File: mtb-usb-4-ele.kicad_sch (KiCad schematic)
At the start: 76 parts, among them J1 USB_C_Receptacle_USB2.0, J2 PROG/DEBUG, J3 Conn_01x06, J4 RJ12, J5 RJ12, J6 Screw_Terminal_01x02, J7 Screw_Terminal_01x02, J8 Conn_01x02, U1 STM32F103C8Tx, U2 AMS1117-3.3, U3 ADM2483xRW, U4 ADUM1250, U6 LM78M05_TO252, U7 INA219AxDCN, Y1 8 MHz

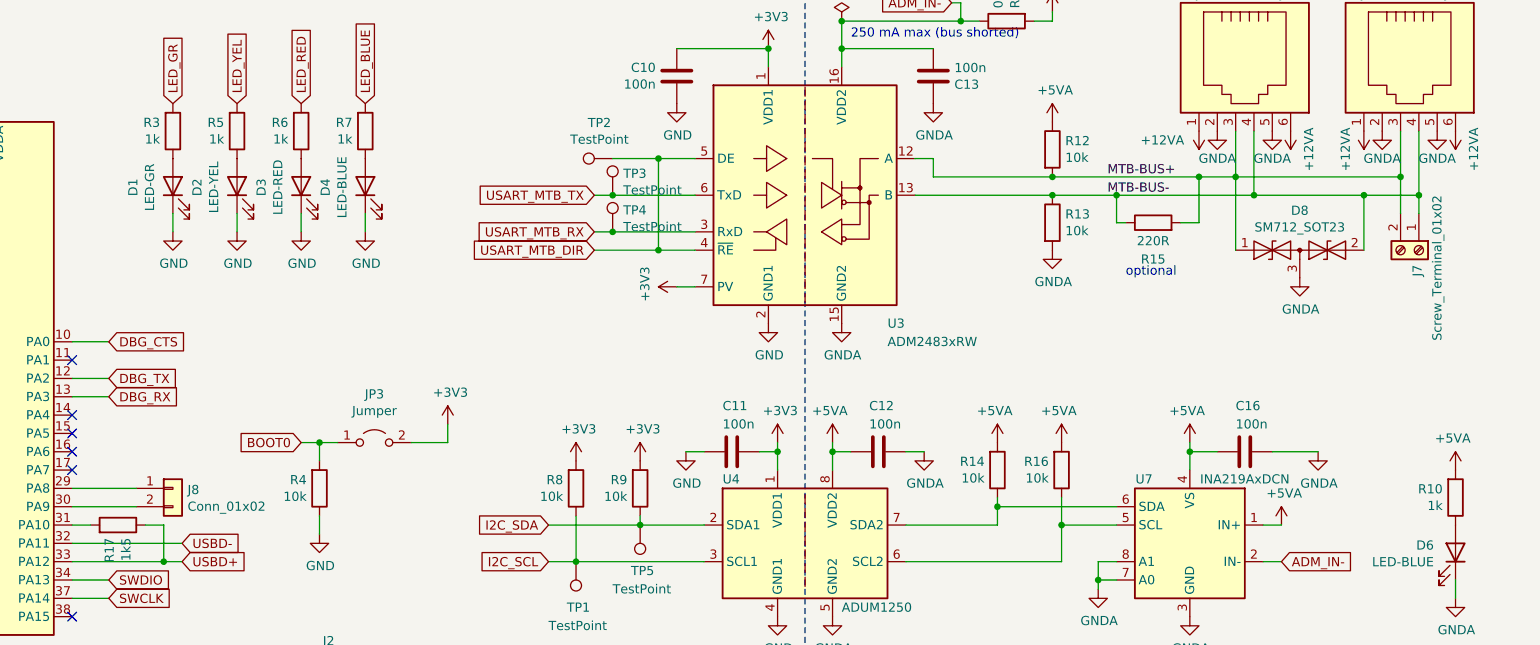
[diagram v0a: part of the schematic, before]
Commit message: Adjust LED resistors.
* 5V blue: 4k7.
* 3V3 blue: 2k2.
* 3V3 green: 10k.
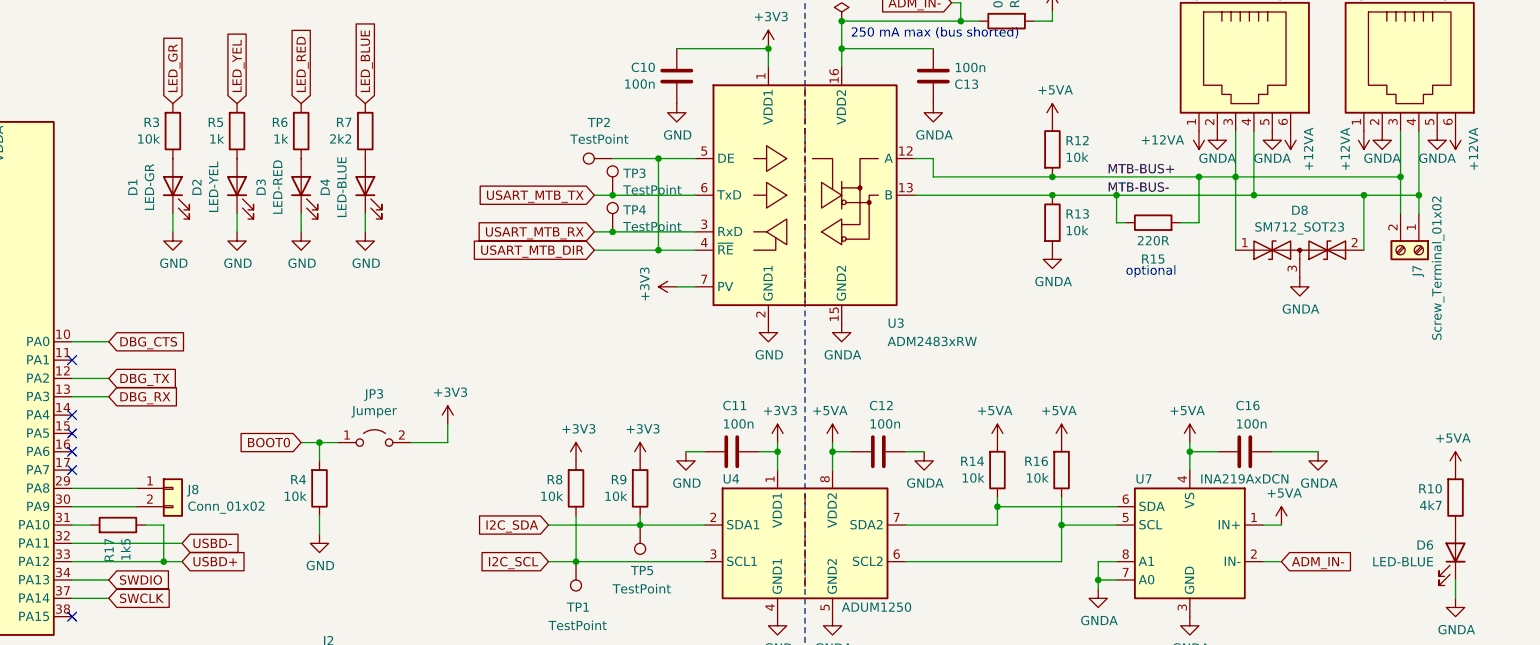
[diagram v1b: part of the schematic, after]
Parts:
- R10: value 1k -> 4k7; LCSC C17513 -> C17673
- R3: value 1k -> 10k; LCSC C17513 -> C17414
- R7: value 1k -> 2k2; LCSC C17513 -> C17520
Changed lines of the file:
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@@
 			)
 		)
-		(property "Value" "1k"
+		(property "Value" "10k"
 			(at 98.552 36.703 0)
 			(effects
@@
 			)
 		)
-		(property "LCSC" "C17513"
+		(property "LCSC" "C17414"
 			(at 100.33 35.56 0)
 			(effects
@@
 			)
 		)
-		(property "Value" "1k"
+		(property "Value" "2k2"
 			(at 125.222 36.703 0)
 			(effects
@@
 			)
 		)
-		(property "LCSC" "C17513"
+		(property "LCSC" "C17520"
 			(at 127 35.56 0)
 			(effects
@@
 			)
 		)
-		(property "Value" "1k"
+		(property "Value" "4k7"
 			(at 276.352 87.503 0)
 			(effects
@@
 			)
 		)
-		(property "LCSC" "C17513"
+		(property "LCSC" "C17673"
 			(at 278.13 86.36 0)
 			(effects

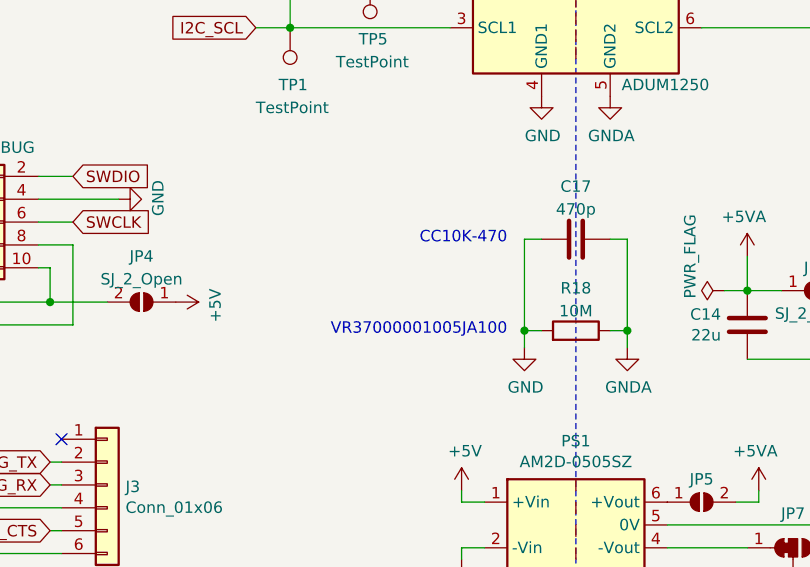
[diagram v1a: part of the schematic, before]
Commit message: TME part id as a part's property.
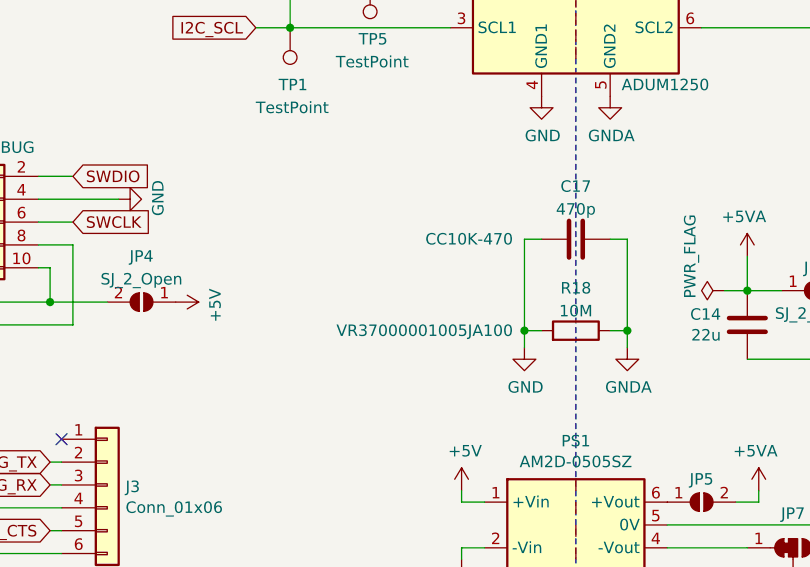
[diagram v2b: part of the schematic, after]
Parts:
- C17: TME (none) -> CC10K-470
- R18: TME (none) -> VR37000001005JA100
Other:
- note removed: "CC10K-470"
- note removed: "VR37000001005JA100"
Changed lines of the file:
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@@
 		)
 	)
-	(text "VR37000001005JA100"
-		(exclude_from_sim no)
-		(at 180.34 129.54 0)
-		(effects
-			(font
-				(size 1.27 1.27)
-			)
-			(justify right bottom)
-		)
-	)
 	(text "optional"
 		(exclude_from_sim no)
@@
 		)
 	)
-	(text "CC10K-470"
-		(exclude_from_sim no)
-		(at 180.34 119.38 0)
-		(effects
-			(font
-				(size 1.27 1.27)
-			)
-			(justify right bottom)
-		)
-	)
 	(label "MTB-BUS+"
 		(at 229.87 41.91 0)
@@
 		(on_board yes)
 		(dnp no)
-		(fields_autoplaced yes)
 		(property "Reference" "C17"
 			(at 187.96 112.8862 90)
@@
 			)
 		)
+		(property "TME" "CC10K-470"
+			(at 180.975 118.745 90)
+			(effects
+				(font
+					(size 1.27 1.27)
+				)
+				(justify left)
+			)
+		)
 		(pin "1"
 		)
@@
 		(on_board yes)
 		(dnp no)
-		(fields_autoplaced yes)
 		(property "Reference" "R18"
 			(at 187.96 124.1892 90)
@@
 			)
 		)
+		(property "TME" "VR37000001005JA100"
+			(at 180.975 128.905 90)
+			(effects
+				(font
+					(size 1.27 1.27)
+				)
+				(justify right)
+			)
+		)

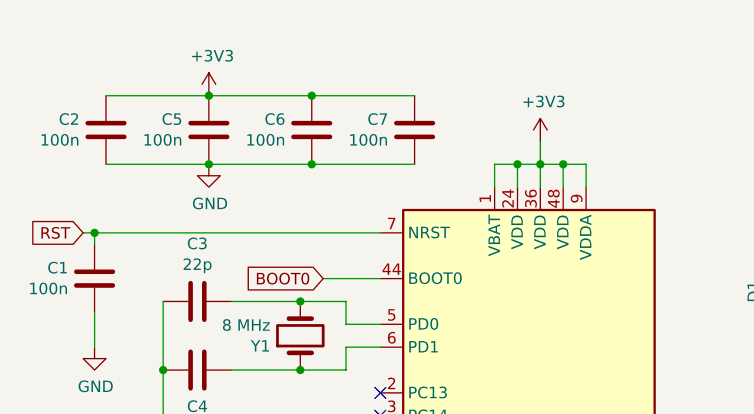
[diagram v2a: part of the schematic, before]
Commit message: MCU: remove power BVAT, VDDA, remove C7.
This board does not have battery and does not use ADC.
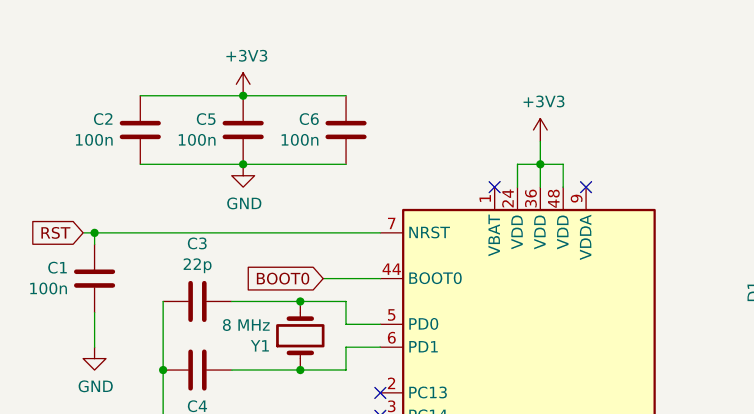
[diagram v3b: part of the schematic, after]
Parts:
- removed C7: 100n, Capacitor_SMD:C_0805_2012Metric, symbol Device:C
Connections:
- net +3V3: no longer U1.1 (VBAT), U1.9 (VDDA)
- no-connect marks 28 -> 30
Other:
- moved on the sheet: C2, C5, C6

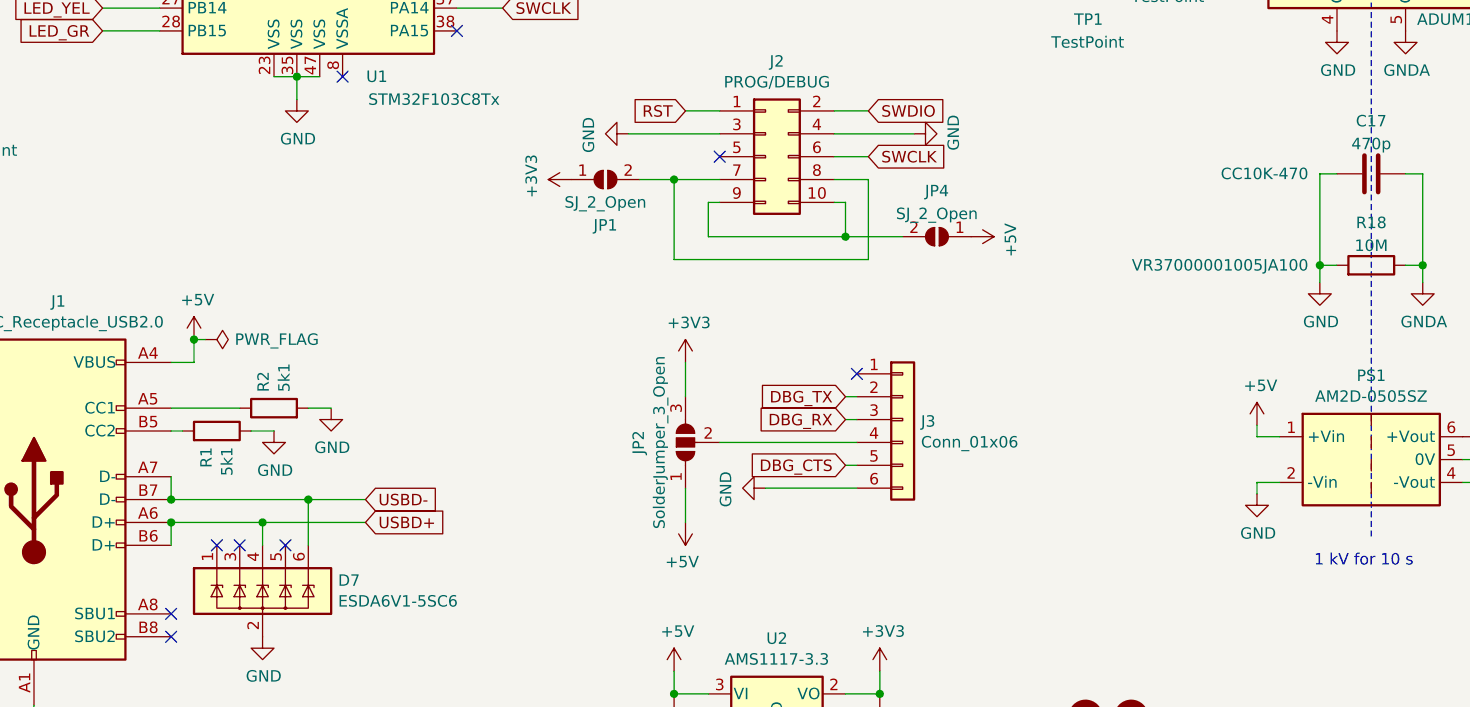
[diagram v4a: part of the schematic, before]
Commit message: Add USB polyfuse 500 mA F1.
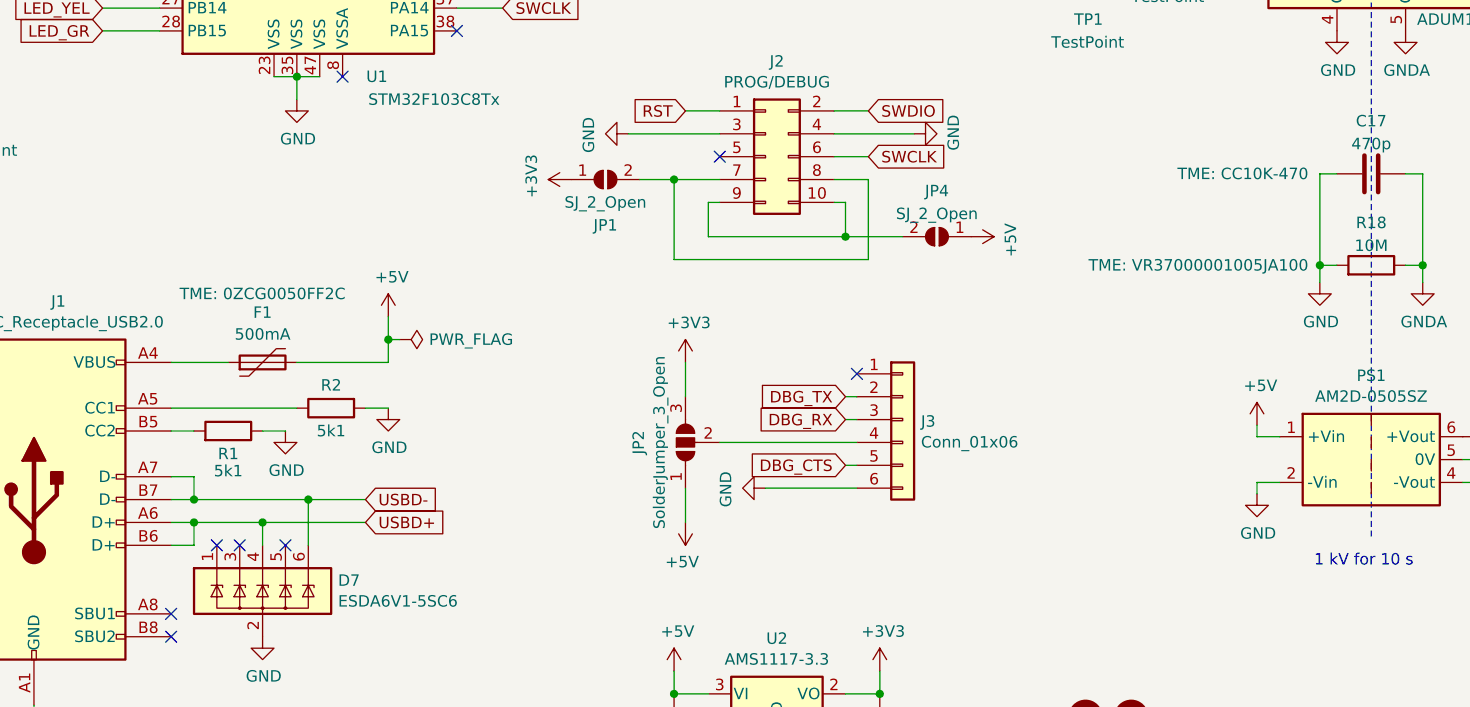
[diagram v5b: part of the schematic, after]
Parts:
- added F1: 500mA, Fuse:Fuse_1812_4532Metric, symbol Device:Polyfuse
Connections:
- net +5V: now also F1.2; no longer J1.A4 (VBUS), J1.A9 (VBUS), J1.B4 (VBUS), J1.B9 (VBUS)
- new net: F1.1, J1.A4 (VBUS), J1.A9 (VBUS), J1.B4 (VBUS), J1.B9 (VBUS)
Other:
- moved on the sheet: R1, R2

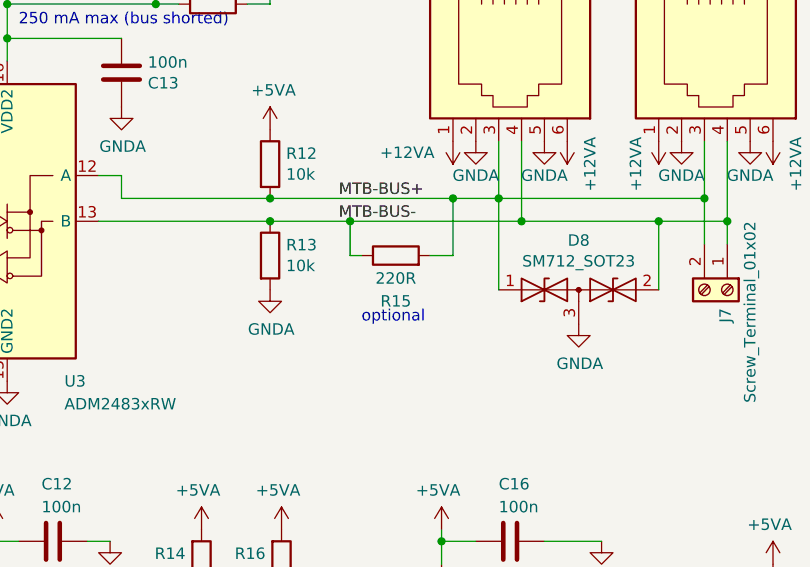
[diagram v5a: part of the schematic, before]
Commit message: Do not populace terminator R15.
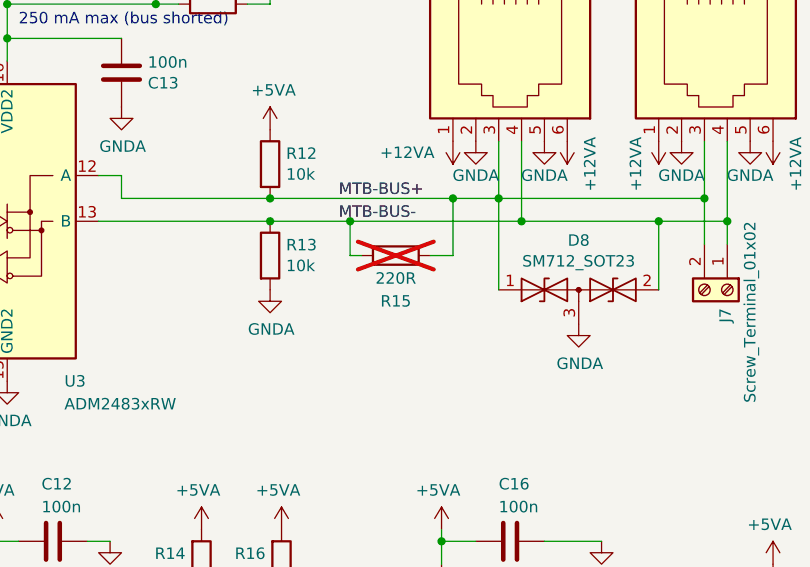
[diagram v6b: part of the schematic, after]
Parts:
- R15: LCSC C17557 -> (none); now not fitted
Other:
- note removed: "optional"
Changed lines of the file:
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@@
 		)
 	)
-	(text "optional"
-		(exclude_from_sim no)
-		(at 232.41 55.88 0)
-		(effects
-			(font
-				(size 1.27 1.27)
-			)
-			(justify left bottom)
-		)
-	)
 	(label "MTB-BUS+"
 		(at 229.87 41.91 0)
@@
 		(in_bom yes)
 		(on_board yes)
-		(dnp no)
+		(dnp yes)
 		(property "Reference" "R15"
 			(at 236.22 53.34 90)
@@
 			(at 236.22 48.26 0)
 			(effects
-				(font
-					(size 1.27 1.27)
-				)
-				(hide yes)
-			)
-		)
-		(property "LCSC" "C17557"
-			(at 236.22 48.26 0)
-			(effects
